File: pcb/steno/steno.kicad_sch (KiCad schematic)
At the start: 63 parts, among them J1 debug-port, K1 diode-choc, K10 diode-choc, K11 diode-choc, K12 diode-choc, K13 diode-choc, K14 diode-choc, K15 diode-choc, K16 diode-choc, K17 diode-choc, K18 diode-choc, K19 diode-choc, K2 diode-choc, K20 diode-choc, K21 diode-choc, K22 diode-choc, K23 diode-choc, K24 diode-choc, K25 diode-choc, K26 diode-choc, K27 diode-choc, K28 diode-choc, K29 diode-choc, K3 diode-choc, K30 diode-choc, K31 diode-choc, K32 diode-choc, K33 diode-choc, K34 diode-choc, K35 diode-choc, K36 diode-choc, K37 diode-choc, K38 diode-choc, K39 diode-choc, K4 diode-choc, K40 diode-choc, K5 diode-choc, K6 diode-choc, K7 diode-choc, K8 diode-choc, K9 diode-choc, Q1 AO3401A, SW2 SW_Push, U1 MT25QL128ABA1ESE, U2 holyiot-18010-no-underside

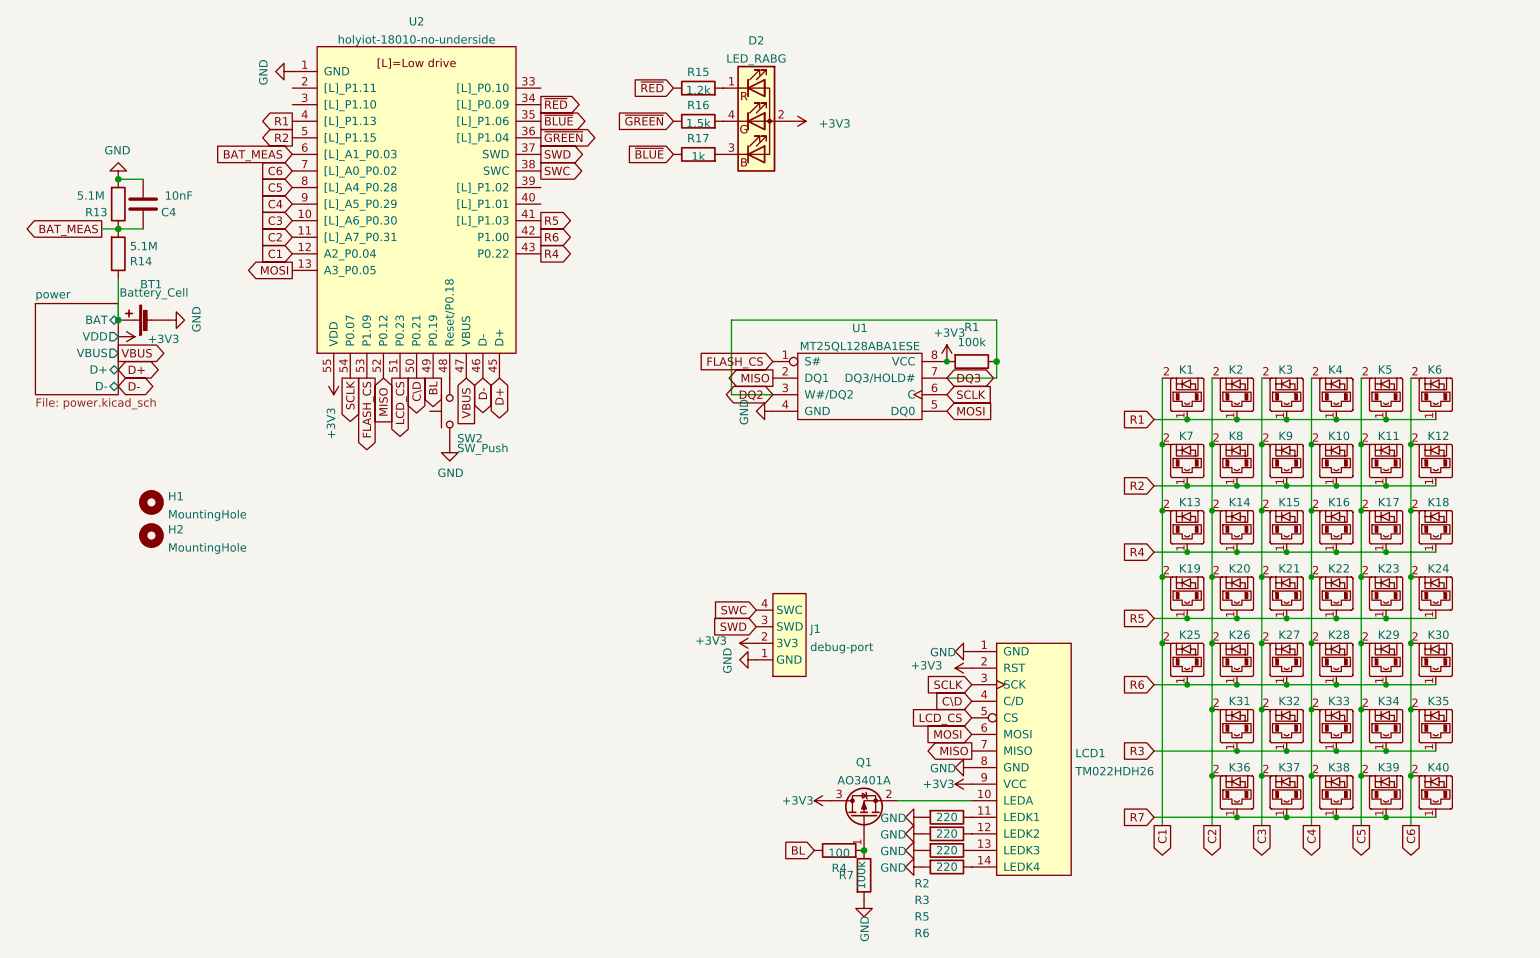
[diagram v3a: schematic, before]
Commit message: fix(auklet): display pin order, routing
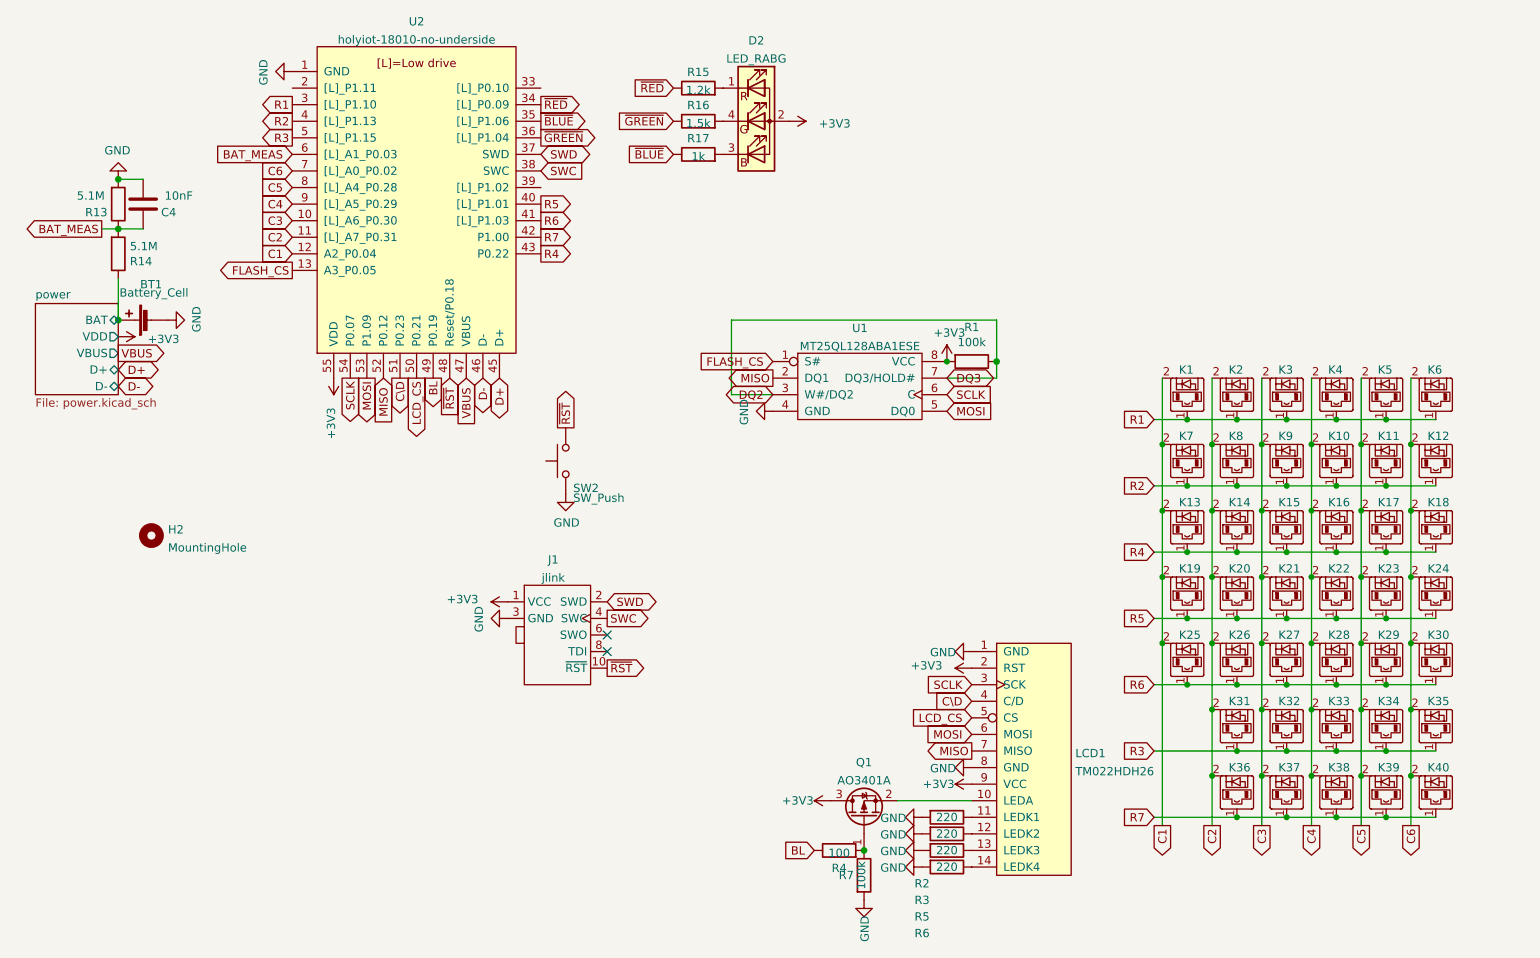
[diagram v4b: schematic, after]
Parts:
- removed H1: MountingHole, misc:auklet-mount, symbol Mechanical:MountingHole
- removed J1: debug-port, misc:debug-port-single-side, symbol misc:debug-port
- added J1: jlink, Connector_PinHeader_1.27mm:PinHeader_2x05_P1.27mm_Vertical_SMD, symbol misc:jlink
- LCD1: footprint display:TM022HDH26 -> display:TM022HDH26_back
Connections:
- net +3V3: now also J1.1 (VCC)
- net C\D: now also U2.51 (P0.23); no longer U2.50 (P0.21)
- net FLASH_CS: now also U2.13 (A3_P0.05); no longer U2.53 (P1.09)
- net GND: now also J1.3 (GND), J1.5 (GND)
- net LCD_CS: now also U2.50 (P0.21); no longer U2.51 (P0.23)
- net MOSI: now also U2.53 (P1.09); no longer U2.13 (A3_P0.05)
- net R1: now also U2.3 ([L]_P1.10); no longer U2.4 ([L]_P1.13)
- net R2: now also U2.4 ([L]_P1.13); no longer U2.5 ([L]_P1.15)
- net R3: now also U2.5 ([L]_P1.15)
- net R5: now also U2.40 ([L]_P1.01); no longer U2.41 ([L]_P1.03)
- net R6: now also U2.41 ([L]_P1.03); no longer U2.42 (P1.00)
- net R7: now also U2.42 (P1.00)
- net SWC: now also J1.4 (SWC)
- net SWD: now also J1.2 (SWD)
- net ~{RST}: now reaches SW2.2, U2.48 (Reset/P0.18)
- net ~{RST}: now also J1.10 (~{RST})
- no-connect marks 0 -> 2
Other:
- moved on the sheet: SW2

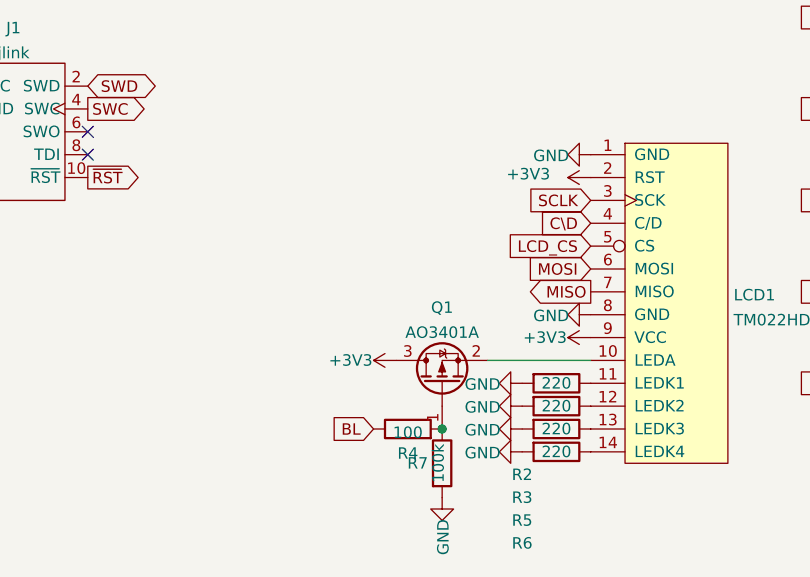
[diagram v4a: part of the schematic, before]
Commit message: fix(auklet): backlight MOSFET
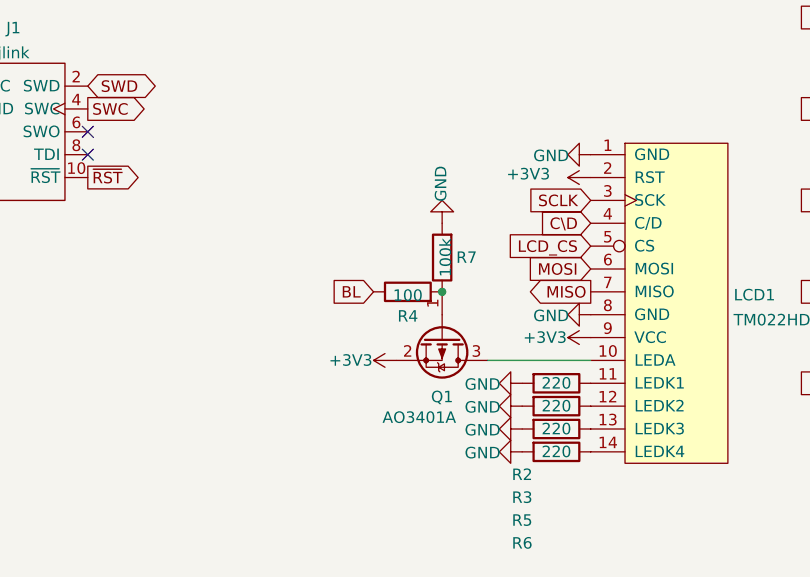
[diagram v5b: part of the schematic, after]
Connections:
- net +3V3: now also Q1.2 (S); no longer Q1.3 (D)
- net at LCD1.10 (LEDA): now also Q1.3 (D); no longer Q1.2 (S)
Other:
- moved on the sheet: Q1, R4, R7
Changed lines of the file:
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@@
   (junction (at 190.5 102.87) (diameter 0) (color 0 0 0 0)
   )
+  (junction (at 144.78 139.7) (diameter 0) (color 0 0 0 0)
+  )
   (junction (at 205.74 113.03) (diameter 0) (color 0 0 0 0)
   )
@@
   )
   (junction (at 205.74 143.51) (diameter 0) (color 0 0 0 0)
-  )
-  (junction (at 144.78 154.94) (diameter 1.016) (color 0 0 0 0)
   )
   (junction (at 228.6 133.35) (diameter 0) (color 0 0 0 0)
@@
     )
   )
-  (global_label "BL" (shape input) (at 137.16 154.94 180) (fields_autoplaced)
-    (effects (font (size 1.27 1.27)) (justify right))
-    (property "Intersheet References" "${INTERSHEET_REFS}" (id 0) (at 132.4488 154.8606 0)
+  (global_label "BL" (shape input) (at 137.16 139.7 180) (fields_autoplaced)
+    (effects (font (size 1.27 1.27)) (justify right))
+    (property "Intersheet References" "${INTERSHEET_REFS}" (id 0) (at 132.4488 139.6206 0)
       (effects (font (size 1.27 1.27)) (justify right) hide)
     )
@@
     (pin "1")
   )
-  (symbol (lib_id "power:GND") (at 144.78 162.56 0) (unit 1)
-    (in_bom yes) (on_board yes)
-    (property "Reference" "#PWR017" (id 0) (at 144.78 168.91 0)
-      (effects (font (size 1.27 1.27)) hide)
-    )
-    (property "Value" "GND" (id 1) (at 144.907 166.9542 90))
-    (property "Footprint" "" (id 2) (at 144.78 162.56 0)
-      (effects (font (size 1.27 1.27)) hide)
-    )
-    (property "Datasheet" "" (id 3) (at 144.78 162.56 0)
+  (symbol (lib_id "power:GND") (at 144.78 132.08 180) (unit 1)
+    (in_bom yes) (on_board yes)
+    (property "Reference" "#PWR017" (id 0) (at 144.78 125.73 0)
+      (effects (font (size 1.27 1.27)) hide)
+    )
+    (property "Value" "GND" (id 1) (at 144.653 127.6858 90))
+    (property "Footprint" "" (id 2) (at 144.78 132.08 0)
+      (effects (font (size 1.27 1.27)) hide)
+    )
+    (property "Datasheet" "" (id 3) (at 144.78 132.08 0)
       (effects (font (size 1.27 1.27)) hide)
     )
@@
     (pin "2")
   )
-  (symbol (lib_id "Device:R") (at 144.78 158.75 0) (unit 1)
-    (in_bom yes) (on_board yes)
-    (property "Reference" "R7" (id 0) (at 142.0622 158.75 0))
-    (property "Value" "100k" (id 1) (at 144.3736 158.75 90))
-    (property "Footprint" "Resistor_SMD:R_0603_1608Metric" (id 2) (at 143.002 158.75 90)
-      (effects (font (size 1.27 1.27)) hide)
-    )
-    (property "Datasheet" "~" (id 3) (at 144.78 158.75 0)
+  (symbol (lib_id "Device:R") (at 144.78 135.89 180) (unit 1)
+    (in_bom yes) (on_board yes)
+    (property "Reference" "R7" (id 0) (at 147.4978 135.89 0))
+    (property "Value" "100k" (id 1) (at 145.1864 135.89 90))
+    (property "Footprint" "Resistor_SMD:R_0603_1608Metric" (id 2) (at 146.558 135.89 90)
+      (effects (font (size 1.27 1.27)) hide)
+    )
+    (property "Datasheet" "~" (id 3) (at 144.78 135.89 0)
       (effects (font (size 1.27 1.27)) hide)
     )
@@
     (pin "2")
   )
-  (symbol (lib_id "Device:R") (at 140.97 154.94 90) (unit 1)
-    (in_bom yes) (on_board yes)
-    (property "Reference" "R4" (id 0) (at 140.97 157.6578 90))
-    (property "Value" "100" (id 1) (at 140.97 155.3464 90))
-    (property "Footprint" "Resistor_SMD:R_0603_1608Metric" (id 2) (at 140.97 156.718 90)
-      (effects (font (size 1.27 1.27)) hide)
-    )
-    (property "Datasheet" "~" (id 3) (at 140.97 154.94 0)
+  (symbol (lib_id "Device:R") (at 140.97 139.7 90) (unit 1)
+    (in_bom yes) (on_board yes)
+    (property "Reference" "R4" (id 0) (at 140.97 142.4178 90))
+    (property "Value" "100" (id 1) (at 140.97 140.1064 90))
+    (property "Footprint" "Resistor_SMD:R_0603_1608Metric" (id 2) (at 140.97 141.478 90)
+      (effects (font (size 1.27 1.27)) hide)
+    )
+    (property "Datasheet" "~" (id 3) (at 140.97 139.7 0)
       (effects (font (size 1.27 1.27)) hide)
     )
@@
     (pin "2")
   )
-  (symbol (lib_id "Transistor_FET:AO3401A") (at 144.78 149.86 90) (unit 1)
-    (in_bom yes) (on_board yes) (fields_autoplaced)
-    (property "Reference" "Q1" (id 0) (at 144.78 141.4484 90))
-    (property "Value" "AO3401A" (id 1) (at 144.78 144.2235 90))
-    (property "Footprint" "Package_TO_SOT_SMD:SOT-23" (id 2) (at 146.685 144.78 0)
+  (symbol (lib_id "Transistor_FET:AO3401A") (at 144.78 144.78 270) (unit 1)
+    (in_bom yes) (on_board yes)
+    (property "Reference" "Q1" (id 0) (at 144.78 151.3745 90))
+    (property "Value" "AO3401A" (id 1) (at 142.24 153.67 90))
+    (property "Footprint" "Package_TO_SOT_SMD:SOT-23" (id 2) (at 142.875 149.86 0)
       (effects (font (size 1.27 1.27) italic) (justify left) hide)
     )
-    (property "Datasheet" "http://www.aosmd.com/pdfs/datasheet/AO3401A.pdf" (id 3) (at 144.78 149.86 0)
-      (effects (font (size 1.27 1.27)) (justify left) hide)
-    )
+    (property "Datasheet" "http://www.aosmd.com/pdfs/datasheet/AO3401A.pdf" (id 3) (at 144.78 144.78 0)
+      (effects (font (size 1.27 1.27)) (justify left) hide)
+    )

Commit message: fix(auklet): update RGB
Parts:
- removed D2: LED_RABG, LED_SMD:LED_ASMB-KTF0-0A306, symbol Device:LED_RABG
- added D2: (no value), symbol Device:LED_BGRA
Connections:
- net +3V3: now also D2.4 (A)
- net at R17.2: now also D2.1 (BK)
- net at R16.2: now also D2.2 (GK)
- net at R15.2: now also D2.3 (RK)
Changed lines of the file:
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@@
     (pin "2")
   )
-  (symbol (lib_id "diode-choc:diode-choc") (at 224.79 85.09 0) (unit 1)
-    (in_bom yes) (on_board yes)
-    (property "Reference" "K5" (id 0) (at 223.52 81.28 0)
-      (effects (font (size 1.27 1.27)) (justify left))
-    )
-    (property "Value" "diode-choc" (id 1) (at 224.79 91.44 0)
-      (effects (font (size 1.27 1.27)) hide)
-    )
-    (property "Footprint" "pg1350:pg1350-D" (id 2) (at 224.79 81.28 0)
-      (effects (font (size 1.27 1.27)) hide)
-    )
-    (property "Datasheet" "" (id 3) (at 224.79 81.28 0)
-      (effects (font (size 1.27 1.27)) hide)
-    )
-    (pin "1")
-    (pin "2")
-  )
-  (symbol (lib_id "diode-choc:diode-choc") (at 224.79 95.25 0) (unit 1)
-    (in_bom yes) (on_board yes)
-    (property "Reference" "K11" (id 0) (at 223.52 91.44 0)
-      (effects (font (size 1.27 1.27)) (justify left))
-    )
-    (property "Value" "diode-choc" (id 1) (at 224.79 101.6 0)
-      (effects (font (size 1.27 1.27)) hide)
-    )
-    (property "Footprint" "pg1350:pg1350-D" (id 2) (at 224.79 91.44 0)
-      (effects (font (size 1.27 1.27)) hide)
-    )
-    (property "Datasheet" "" (id 3) (at 224.79 91.44 0)
-      (effects (font (size 1.27 1.27)) hide)
-    )
-    (pin "1")
-    (pin "2")
-  )
-  (symbol (lib_id "Device:LED_RABG") (at 128.27 43.18 0) (unit 1)
-    (in_bom no) (on_board yes) (fields_autoplaced)
-    (property "Reference" "D2" (id 0) (at 128.27 30.8314 0))
-    (property "Value" "LED_RABG" (id 1) (at 128.27 33.6065 0))
-    (property "Footprint" "LED_SMD:LED_ASMB-KTF0-0A306" (id 2) (at 128.27 44.45 0)
+  (symbol (lib_id "Device:LED_BGRA") (at 128.27 43.18 0) (unit 1)
+    (in_bom yes) (on_board yes) (fields_autoplaced)
+    (property "Reference" "D2" (id 0) (at 128.27 31.0982 0))
+    (property "Value" "" (id 1) (at 128.27 33.6351 0))
+    (property "Footprint" "" (id 2) (at 128.27 44.45 0)
       (effects (font (size 1.27 1.27)) hide)
     )
@@
     (pin "3")
     (pin "4")
+  )
+  (symbol (lib_id "diode-choc:diode-choc") (at 224.79 85.09 0) (unit 1)
+    (in_bom yes) (on_board yes)
+    (property "Reference" "K5" (id 0) (at 223.52 81.28 0)
+      (effects (font (size 1.27 1.27)) (justify left))
+    )
+    (property "Value" "diode-choc" (id 1) (at 224.79 91.44 0)
+      (effects (font (size 1.27 1.27)) hide)
+    )
+    (property "Footprint" "pg1350:pg1350-D" (id 2) (at 224.79 81.28 0)
+      (effects (font (size 1.27 1.27)) hide)
+    )
+    (property "Datasheet" "" (id 3) (at 224.79 81.28 0)
+      (effects (font (size 1.27 1.27)) hide)
+    )
+    (pin "1")
+    (pin "2")
+  )
+  (symbol (lib_id "diode-choc:diode-choc") (at 224.79 95.25 0) (unit 1)
+    (in_bom yes) (on_board yes)
+    (property "Reference" "K11" (id 0) (at 223.52 91.44 0)
+      (effects (font (size 1.27 1.27)) (justify left))
+    )
+    (property "Value" "diode-choc" (id 1) (at 224.79 101.6 0)
+      (effects (font (size 1.27 1.27)) hide)
+    )
+    (property "Footprint" "pg1350:pg1350-D" (id 2) (at 224.79 91.44 0)
+      (effects (font (size 1.27 1.27)) hide)
+    )
+    (property "Datasheet" "" (id 3) (at 224.79 91.44 0)
+      (effects (font (size 1.27 1.27)) hide)
+    )
+    (pin "1")
+    (pin "2")
   )
   (symbol (lib_id "diode-choc:diode-choc") (at 224.79 105.41 0) (unit 1)
@@
       (reference "D1") (unit 1) (value "RED") (footprint "LED_SMD:LED_0805_2012Metric")
     )
-    (path "/c834c310-715e-4686-b6c7-8c5db7cbfe1a"
-      (reference "D2") (unit 1) (value "LED_RABG") (footprint "LED_SMD:LED_ASMB-KTF0-0A306")
+    (path "/ad881e84-05e1-488e-a9dd-6c40065bc6b5"
+      (reference "D2") (unit 1) (value "LED_BGRA") (footprint "LED_SMD:LED_ASMB-KTF0-0A306")
     )
     (path "/6ec6d3f2-728d-4612-8023-db52c913d770"
